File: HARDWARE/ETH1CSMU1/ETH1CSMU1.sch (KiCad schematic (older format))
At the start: 0 parts

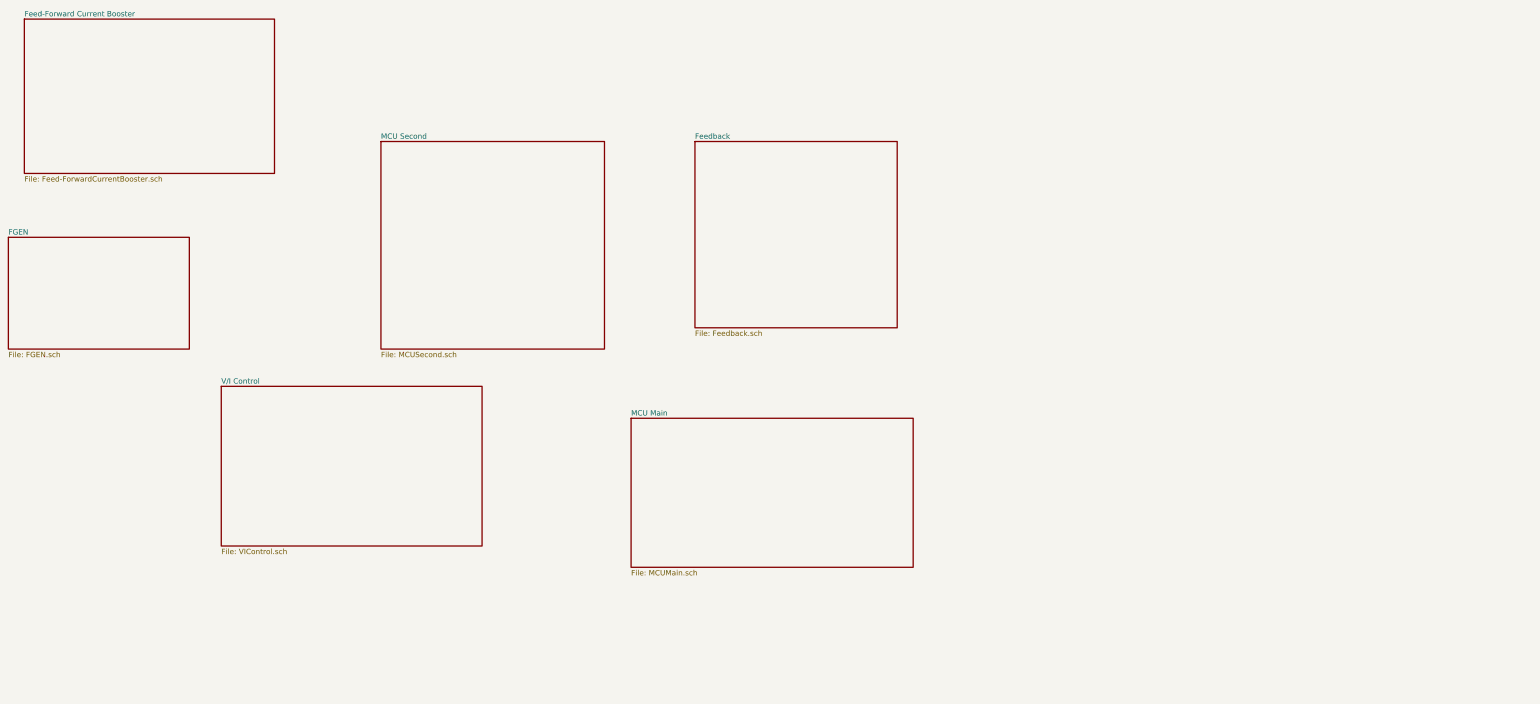
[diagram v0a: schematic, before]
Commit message: Added ADC
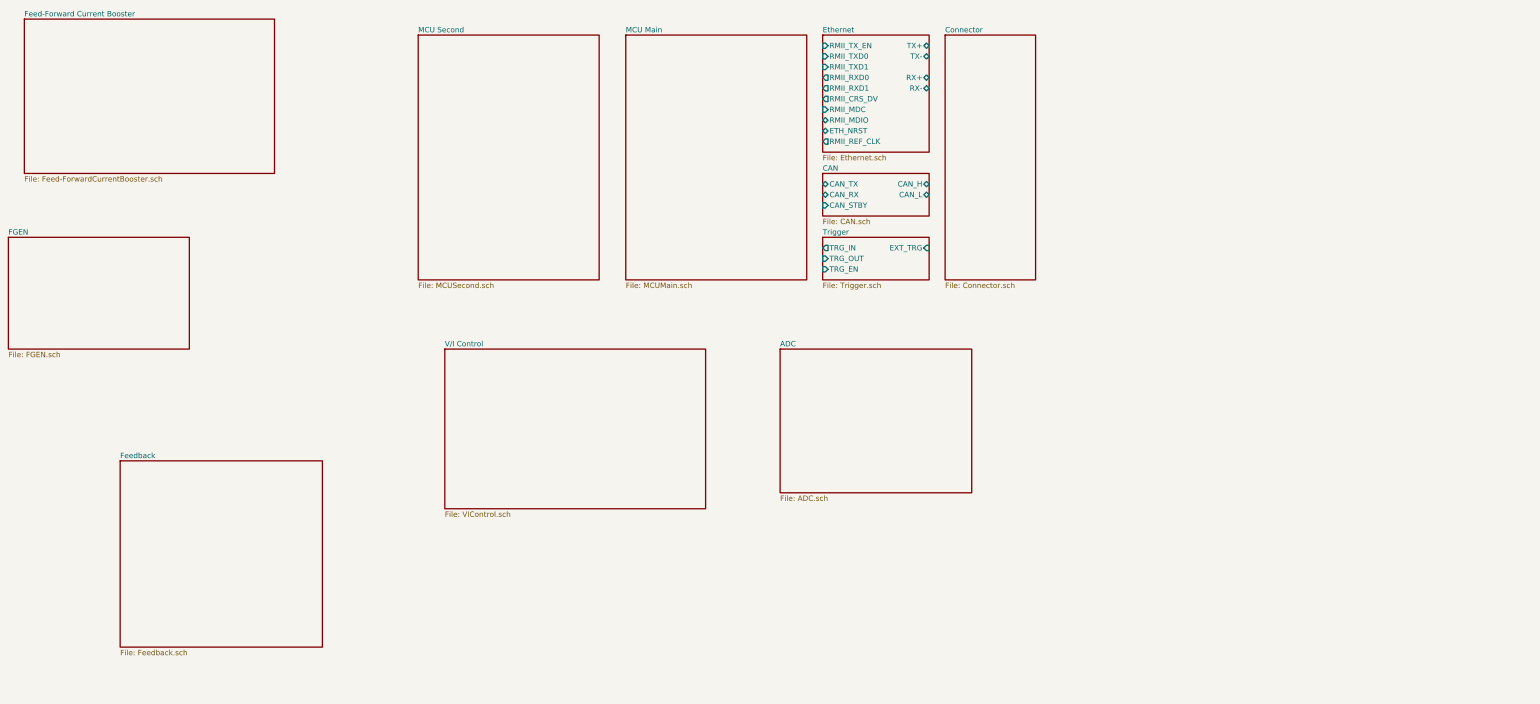
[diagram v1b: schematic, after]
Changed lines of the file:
@@
 EESchema Schematic File Version 4
+LIBS:ETH1CSMU1-cache
 EELAYER 26 0
 EELAYER END
 $Descr A4 11693 8268
 encoding utf-8
-Sheet 1 7
+Sheet 1 12
 Title ""
 Date ""
@@
 $EndDescr
 $Sheet
-S 4750 2250 2100 1950
+S 5100 1250 1700 2300
 U 5BE0F4FE
 F0 "MCU Second" 50
@@
 $EndSheet
 $Sheet
-S 7700 2250 1900 1750
+S 2300 5250 1900 1750
 U 5BE150E7
 F0 "Feedback" 50
@@
 $EndSheet
 $Sheet
-S 3250 4550 2450 1500
+S 5350 4200 2450 1500
 U 5BE1CBE6
 F0 "V/I Control" 50
@@
 $EndSheet
 $Sheet
-S 7100 4850 2650 1400
+S 7050 1250 1700 2300
 U 5BE4235D
 F0 "MCU Main" 50
 F1 "MCUMain.sch" 50
 $EndSheet
+$Sheet
+S 8900 2550 1000 400
+U 5BE10334
+F0 "CAN" 50
+F1 "CAN.sch" 50
+F2 "CAN_TX" B L 8900 2650 50
+F3 "CAN_RX" B L 8900 2750 50
+F4 "CAN_STBY" I L 8900 2850 50
+F5 "CAN_H" B R 9900 2650 50
+F6 "CAN_L" B R 9900 2750 50
+$EndSheet
+$Sheet
+S 8900 3150 1000 400
+U 5BE1246B
+F0 "Trigger" 50
+F1 "Trigger.sch" 50
+F2 "TRG_IN" O L 8900 3250 50
+F3 "TRG_OUT" I L 8900 3350 50
+F4 "TRG_EN" I L 8900 3450 50
+F5 "EXT_TRG" I R 9900 3250 50
+$EndSheet
+$Sheet
+S 8900 1250 1000 1100
+U 5BE18CAF
+F0 "Ethernet" 50
+F1 "Ethernet.sch" 50
+F2 "TX+" B R 9900 1350 50
+F3 "TX-" B R 9900 1450 50
+F4 "RX+" B R 9900 1650 50
+F5 "RX-" B R 9900 1750 50
+F6 "RMII_TX_EN" I L 8900 1350 50
+F7 "RMII_TXD0" I L 8900 1450 50
+F8 "RMII_TXD1" I L 8900 1550 50
+F9 "RMII_RXD0" O L 8900 1650 50
+F10 "RMII_RXD1" O L 8900 1750 50
+F11 "RMII_CRS_DV" O L 8900 1850 50
+F12 "RMII_MDC" I L 8900 1950 50
+F13 "RMII_MDIO" B L 8900 2050 50
+F14 "ETH_NRST" B L 8900 2150 50
+F15 "RMII_REF_CLK" O L 8900 2250 50
+$EndSheet
+$Sheet
+S 10050 1250 850  2300
+U 5BE2F1B8
+F0 "Connector" 50
+F1 "Connector.sch" 50
+$EndSheet
+$Sheet
+S 8500 4200 1800 1350
+U 5C548E81
+F0 "ADC" 50
+F1 "ADC.sch" 50
+$EndSheet
 $EndSCHEMATC

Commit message: Commit
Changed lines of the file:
@@
 EELAYER 26 0
 EELAYER END
-$Descr A4 11693 8268
+$Descr A3 16535 11693
 encoding utf-8
 Sheet 1 12
@@
 $EndDescr
 $Sheet
-S 5100 1250 1700 2300
+S 9550 3350 1750 3950
 U 5BE0F4FE
 F0 "MCU Second" 50
@@
 $EndSheet
 $Sheet
-S 2300 5250 1900 1750
+S 2600 5100 1900 1750
 U 5BE150E7
 F0 "Feedback" 50
@@
 $EndSheet
 $Sheet
-S 5350 4200 2450 1500
+S 5450 3350 1350 1800
 U 5BE1CBE6
 F0 "V/I Control" 50
@@
 $EndSheet
 $Sheet
-S 1400 1100 2350 1450
+S 2600 3350 2350 1450
 U 5BE35C2A
 F0 "Feed-Forward Current Booster" 50
@@
 $EndSheet
 $Sheet
-S 1250 3150 1700 1050
+S 7550 3350 1250 1500
 U 5BE3BF24
 F0 "FGEN" 50
 F1 "FGEN.sch" 50
+F2 "FGEN_SCLK" I R 8800 3450 50
+F3 "FGEN_SDATA" I R 8800 3550 50
+F4 "FGEN_~FSYNC" I R 8800 3650 50
+F5 "FGEN_SLEEP" I R 8800 3750 50
+F6 "FGEN_PSELECT" I R 8800 3850 50
+F7 "FGEN_FSELECT" I R 8800 3950 50
+F8 "FGEN" O L 7550 3450 50
+F9 "FGEN_MDAC_~SYNC" I R 8800 4150 50
+F10 "FGEN_OFFS_~SYNC" I R 8800 4650 50
+F11 "FGEN_OFFS_SCKL" I R 8800 4750 50
+F12 "FGEN_OFFS_DIN" I R 8800 4550 50
+F13 "FGEN_MDAC_SDIN" I R 8800 4250 50
+F14 "FGEN_MDAC_SCLK" I R 8800 4350 50
 $EndSheet
 $Sheet
-S 7050 1250 1700 2300
+S 11500 3350 1750 3950
 U 5BE4235D
 F0 "MCU Main" 50
 F1 "MCUMain.sch" 50
+F2 "RMII_TX_EN" O R 13250 3450 50
+F3 "RMII_TXD0" O R 13250 3550 50
+F4 "RMII_TXD1" O R 13250 3650 50
+F5 "RMII_RXD0" I R 13250 3750 50
+F6 "RMII_RXD1" I R 13250 3850 50
+F7 "RMII_CRS_DV" I R 13250 3950 50
+F8 "RMII_MDC" O R 13250 4050 50
+F9 "RMII_MDIO" B R 13250 4150 50
+F10 "ETH_NRST" B R 13250 4250 50
+F11 "RMII_REF_CLK" I R 13250 4350 50
+F12 "CAN1_RX" B R 13250 4850 50
+F13 "CAN1_TX" B R 13250 4750 50
+F14 "CAN_STBY" O R 13250 4950 50
 $EndSheet
 $Sheet
-S 8900 2550 1000 400
+S 13450 4650 1000 400
 U 5BE10334
 F0 "CAN" 50
 F1 "CAN.sch" 50
-F2 "CAN_TX" B L 8900 2650 50
-F3 "CAN_RX" B L 8900 2750 50
-F4 "CAN_STBY" I L 8900 2850 50
-F5 "CAN_H" B R 9900 2650 50
-F6 "CAN_L" B R 9900 2750 50
+F2 "CAN_TX" B L 13450 4750 50
+F3 "CAN_RX" B L 13450 4850 50
+F4 "CAN_STBY" I L 13450 4950 50
+F5 "CAN_H" B R 14450 4750 50
+F6 "CAN_L" B R 14450 4850 50
 $EndSheet
 $Sheet
-S 8900 3150 1000 400
+S 13450 5250 1000 400
 U 5BE1246B
 F0 "Trigger" 50
 F1 "Trigger.sch" 50
-F2 "TRG_IN" O L 8900 3250 50
-F3 "TRG_OUT" I L 8900 3350 50
-F4 "TRG_EN" I L 8900 3450 50
-F5 "EXT_TRG" I R 9900 3250 50
+F2 "TRG_IN" O L 13450 5350 50
+F3 "TRG_OUT" I L 13450 5450 50
+F4 "TRG_EN" I L 13450 5550 50
+F5 "EXT_TRG" I R 14450 5350 50
 $EndSheet
 $Sheet
-S 8900 1250 1000 1100
+S 13450 3350 1000 1100
 U 5BE18CAF
 F0 "Ethernet" 50
 F1 "Ethernet.sch" 50
-F2 "TX+" B R 9900 1350 50
-F3 "TX-" B R 9900 1450 50
-F4 "RX+" B R 9900 1650 50
-F5 "RX-" B R 9900 1750 50
-F6 "RMII_TX_EN" I L 8900 1350 50
-F7 "RMII_TXD0" I L 8900 1450 50
-F8 "RMII_TXD1" I L 8900 1550 50
-F9 "RMII_RXD0" O L 8900 1650 50
-F10 "RMII_RXD1" O L 8900 1750 50
-F11 "RMII_CRS_DV" O L 8900 1850 50
-F12 "RMII_MDC" I L 8900 1950 50
-F13 "RMII_MDIO" B L 8900 2050 50
-F14 "ETH_NRST" B L 8900 2150 50
-F15 "RMII_REF_CLK" O L 8900 2250 50
+F2 "TX+" B R 14450 3450 50
+F3 "TX-" B R 14450 3550 50
+F4 "RX+" B R 14450 3750 50
+F5 "RX-" B R 14450 3850 50
+F6 "RMII_TX_EN" I L 13450 3450 50
+F7 "RMII_TXD0" I L 13450 3550 50
+F8 "RMII_TXD1" I L 13450 3650 50
+F9 "RMII_RXD0" O L 13450 3750 50
+F10 "RMII_RXD1" O L 13450 3850 50
+F11 "RMII_CRS_DV" O L 13450 3950 50
+F12 "RMII_MDC" I L 13450 4050 50
+F13 "RMII_MDIO" B L 13450 4150 50
+F14 "ETH_NRST" B L 13450 4250 50
+F15 "RMII_REF_CLK" O L 13450 4350 50
 $EndSheet
 $Sheet
-S 10050 1250 850  2300
+S 14650 3350 750  2300
 U 5BE2F1B8
 F0 "Connector" 50
@@
 $EndSheet
 $Sheet
-S 8500 4200 1800 1350
+S 7550 5150 1550 1650
 U 5C548E81
 F0 "ADC" 50
 F1 "ADC.sch" 50
+F2 "ADC_SEL0" I R 9100 5250 50
+F3 "ADC_SEL1" I R 9100 5350 50
+F4 "ADC_SYNC" I R 9100 5450 50
+F5 "ADC_~RDLA" I R 9100 5550 50
+F6 "ADC_~RDLB" I R 9100 5650 50
+F7 "ADC_~DRL" O R 9100 5750 50
+F8 "ADC_BUSY" O R 9100 5850 50
+F9 "ADC_SCK" B R 9100 5950 50
+F10 "ADC_SDO" O R 9100 6050 50
+F11 "ADC_MCLK" I R 9100 6150 50
+F12 "CURRENT_FEEDBACK" I L 7550 5250 50
+F13 "VOLTAGE_FEEDBACK" I L 7550 5350 50
+F14 "ADC_MUX_A0" I R 9100 6250 50
+F15 "ADC_MUX_A1" I R 9100 6350 50
+F16 "ADC_MUX_EN" I R 9100 6450 50
+F17 "REF+10V" I L 7550 5450 50
 $EndSheet
+Wire Wire Line
+	13250 3450 13450 3450
+Wire Wire Line
+	13450 3550 13250 3550
+Wire Wire Line
+	13250 3650 13450 3650
+Wire Wire Line
+	13450 3750 13250 3750
+Wire Wire Line
+	13250 3850 13450 3850
+Wire Wire Line
+	13450 3950 13250 3950
+Wire Wire Line
+	13250 4050 13450 4050
+Wire Wire Line
+	13250 4150 13450 4150
+Wire Wire Line
+	13450 4250 13250 4250
+Wire Wire Line
+	13250 4350 13450 4350
+Wire Wire Line
+	13250 4750 13450 4750
+Wire Wire Line
+	13450 4850 13250 4850
+Wire Wire Line
+	13250 4950 13450 4950
 $EndSCHEMATC

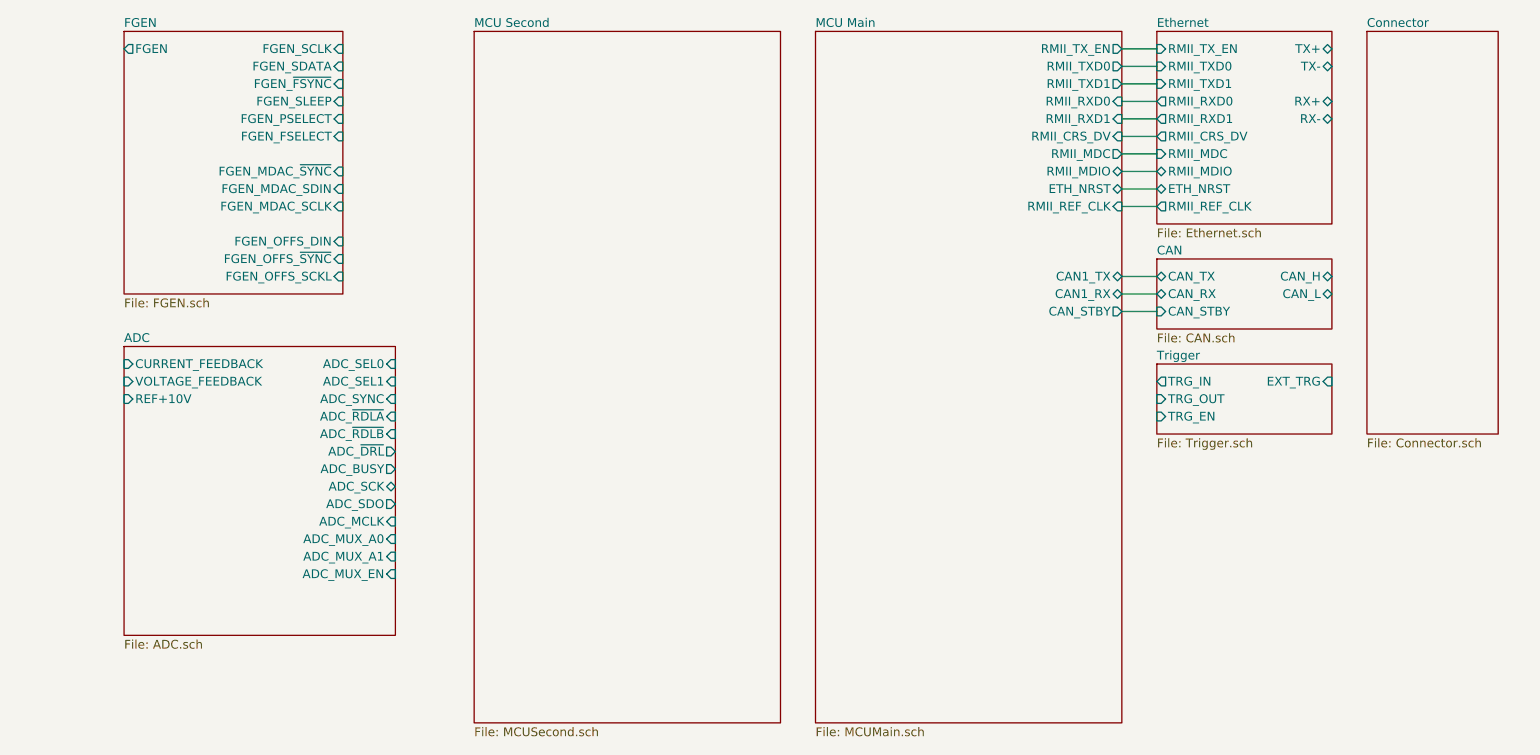
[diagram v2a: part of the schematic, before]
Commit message: Power schematic
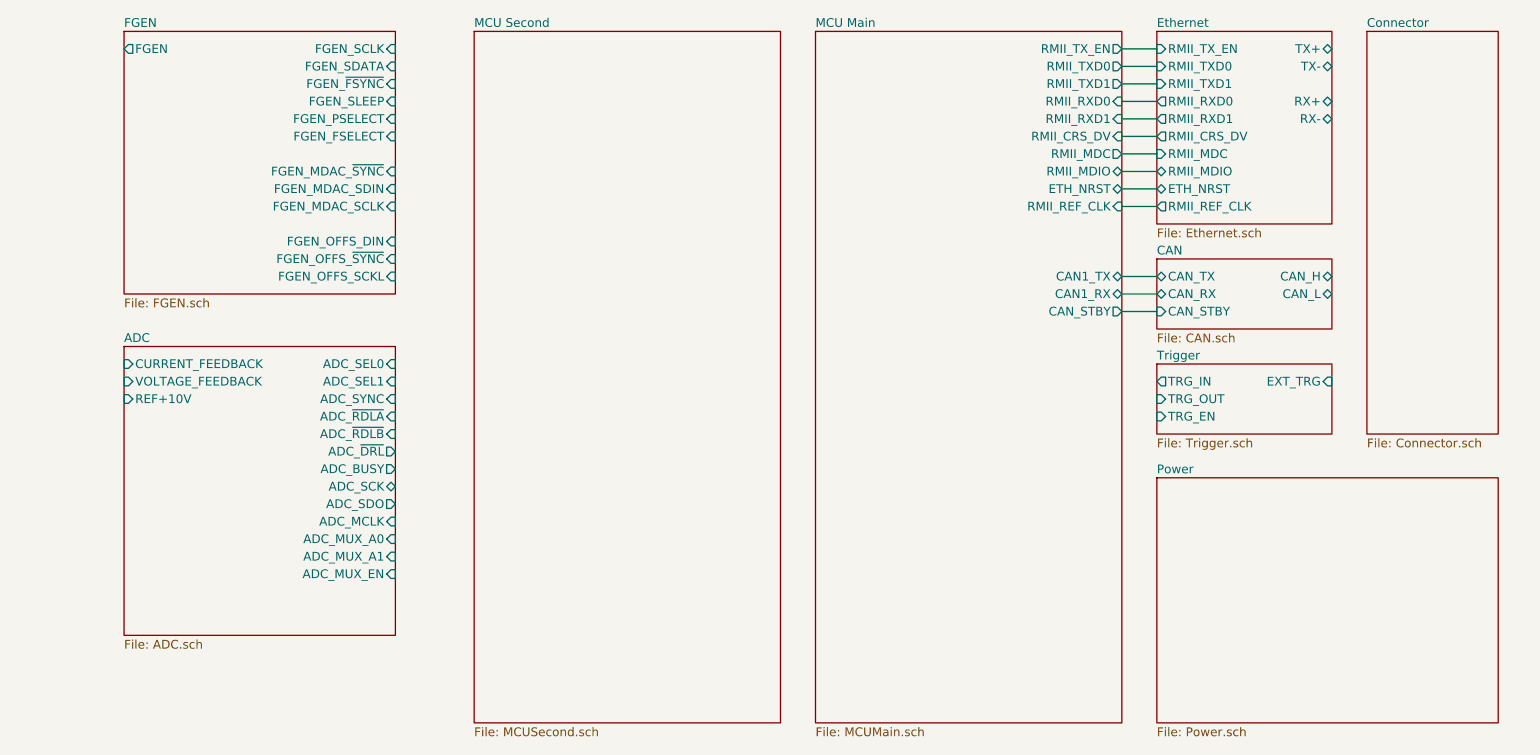
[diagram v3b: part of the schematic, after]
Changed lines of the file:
@@
 $Descr A3 16535 11693
 encoding utf-8
-Sheet 1 12
+Sheet 1 13
 Title ""
 Date ""
@@
 $EndSheet
 $Sheet
-S 7550 3350 1250 1500
+S 7550 3350 1550 1500
 U 5BE3BF24
 F0 "FGEN" 50
 F1 "FGEN.sch" 50
-F2 "FGEN_SCLK" I R 8800 3450 50
-F3 "FGEN_SDATA" I R 8800 3550 50
-F4 "FGEN_~FSYNC" I R 8800 3650 50
-F5 "FGEN_SLEEP" I R 8800 3750 50
-F6 "FGEN_PSELECT" I R 8800 3850 50
-F7 "FGEN_FSELECT" I R 8800 3950 50
+F2 "FGEN_SCLK" I R 9100 3450 50
+F3 "FGEN_SDATA" I R 9100 3550 50
+F4 "FGEN_~FSYNC" I R 9100 3650 50
+F5 "FGEN_SLEEP" I R 9100 3750 50
+F6 "FGEN_PSELECT" I R 9100 3850 50
+F7 "FGEN_FSELECT" I R 9100 3950 50
 F8 "FGEN" O L 7550 3450 50
-F9 "FGEN_MDAC_~SYNC" I R 8800 4150 50
-F10 "FGEN_OFFS_~SYNC" I R 8800 4650 50
-F11 "FGEN_OFFS_SCKL" I R 8800 4750 50
-F12 "FGEN_OFFS_DIN" I R 8800 4550 50
-F13 "FGEN_MDAC_SDIN" I R 8800 4250 50
-F14 "FGEN_MDAC_SCLK" I R 8800 4350 50
+F9 "FGEN_MDAC_~SYNC" I R 9100 4150 50
+F10 "FGEN_OFFS_~SYNC" I R 9100 4650 50
+F11 "FGEN_OFFS_SCKL" I R 9100 4750 50
+F12 "FGEN_OFFS_DIN" I R 9100 4550 50
+F13 "FGEN_MDAC_SDIN" I R 9100 4250 50
+F14 "FGEN_MDAC_SCLK" I R 9100 4350 50
 $EndSheet
 $Sheet
@@
 Wire Wire Line
 	13250 4950 13450 4950
+$Sheet
+S 13450 5900 1950 1400
+U 5BF5DBE2
+F0 "Power" 50
+F1 "Power.sch" 50
+$EndSheet
 $EndSCHEMATC
